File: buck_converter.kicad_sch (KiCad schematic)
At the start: 42 parts, among them IC2 LM34936RHFR, Q10 CSD15571Q2, Q11 CSD15571Q2, Q5 CSD17571Q2, Q6 CSD15571Q2, Q9 CSD17571Q2

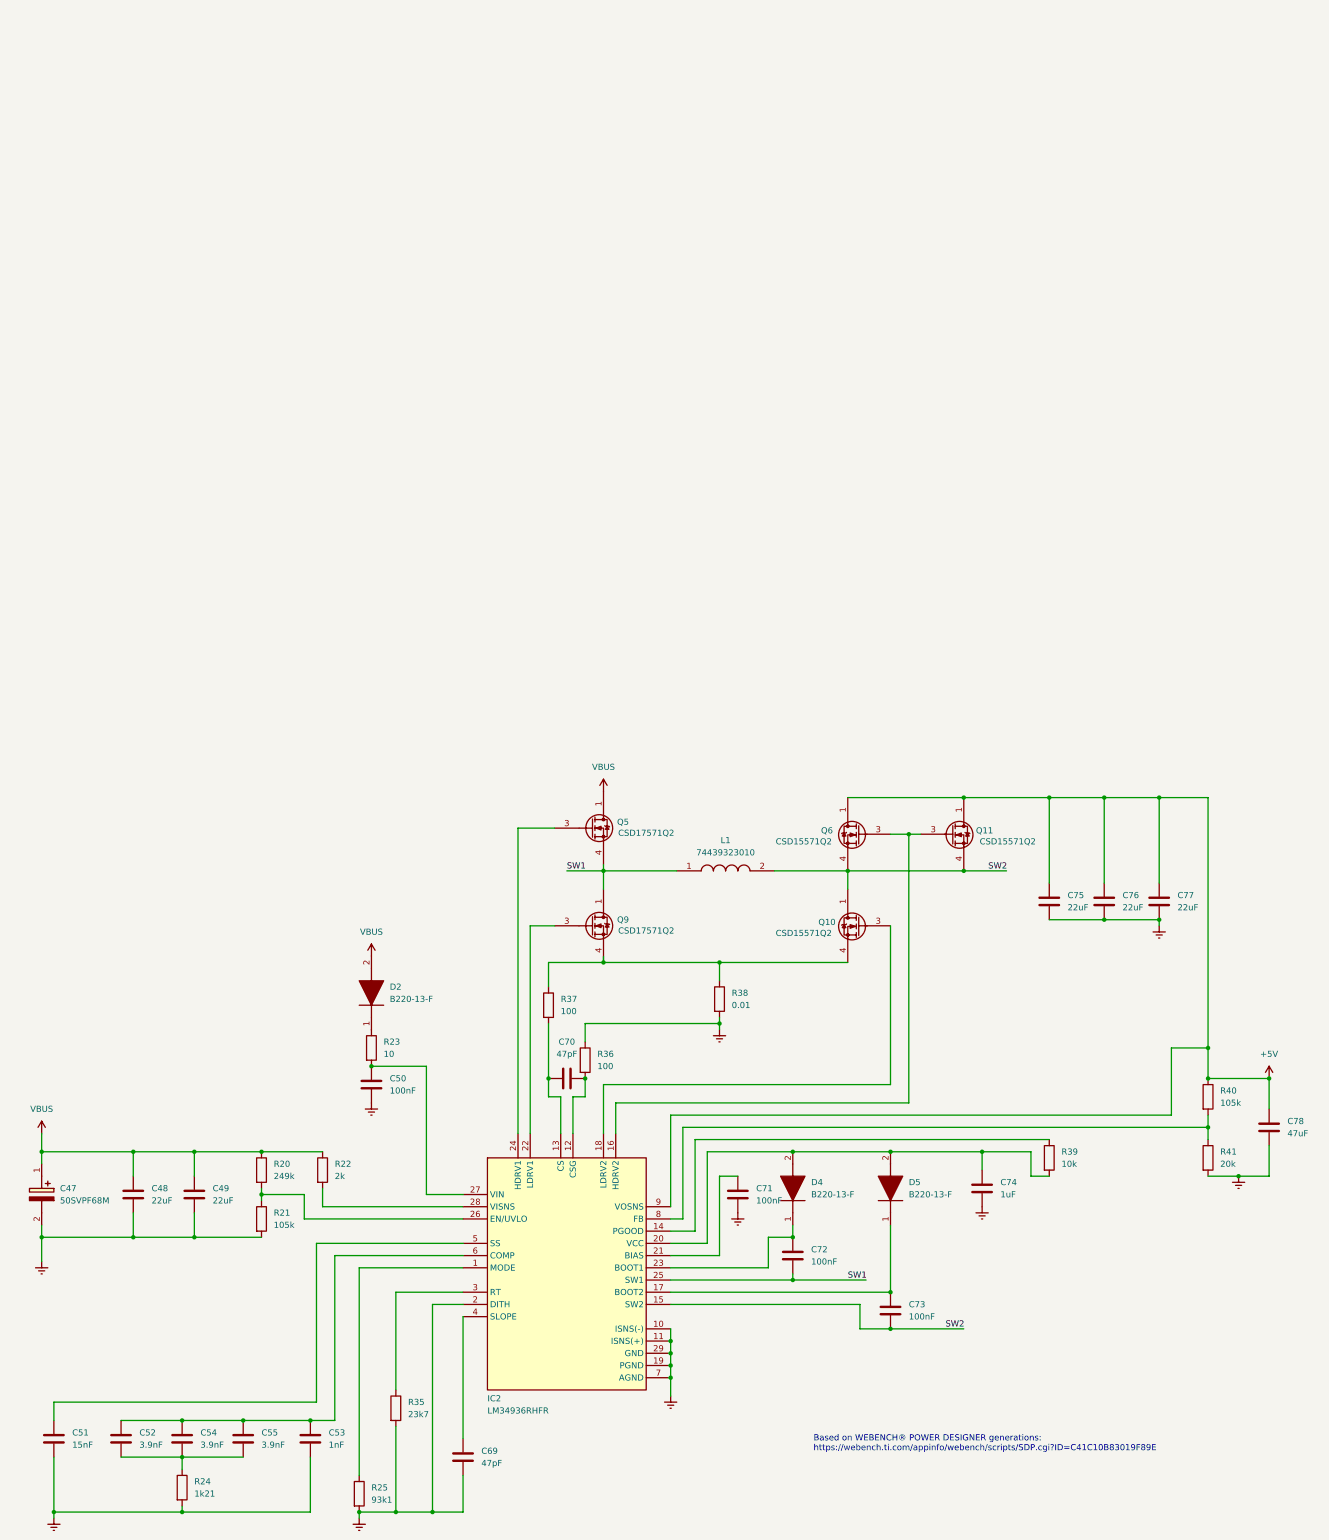
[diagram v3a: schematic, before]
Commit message: annotation and pcb outline
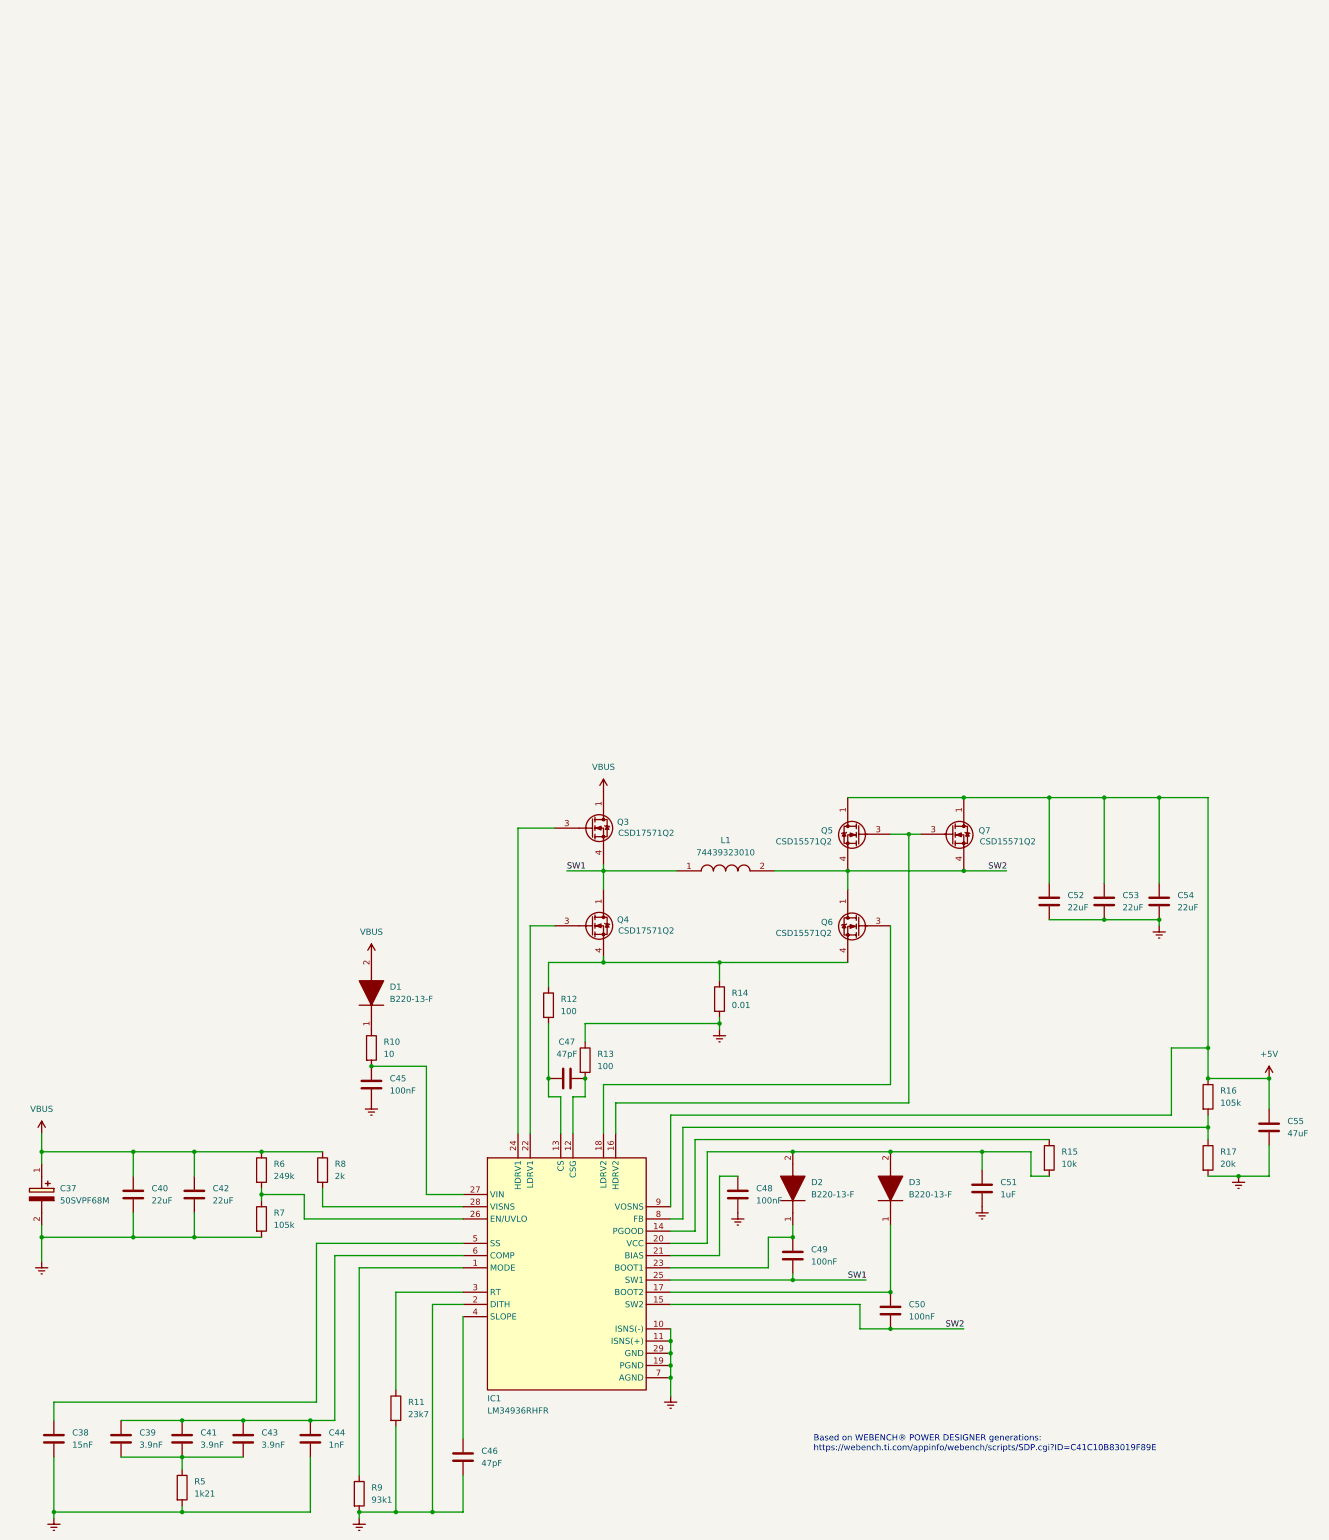
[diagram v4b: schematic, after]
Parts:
- Q5: renamed from Q6; footprint CSD15571Q2 -> CSD15571Q2:CSD15571Q2
- renumbered C47 to C37, C51 to C38, C52 to C39, C48 to C40, C54 to C41, C49 to C42, C55 to C43, C53 to C44, C50 to C45, C69 to C46, C70 to C47, C71 to C48, C72 to C49, C73 to C50, C74 to C51, C75 to C52, C76 to C53, C77 to C54, C78 to C55, D2 to D1, D4 to D2, D5 to D3, IC2 to IC1, Q5 to Q3, Q9 to Q4, Q10 to Q6, Q11 to Q7, R23 to R10, R35 to R11, R37 to R12, R36 to R13, R38 to R14, R39 to R15, R40 to R16, R41 to R17, R24 to R5, R20 to R6, R21 to R7, R22 to R8, R25 to R9

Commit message: new caps and bit of layout
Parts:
- removed C37: 50SVPF68M, 50SVPF68M:16SVF1000M, symbol 50SVPF68M:50SVPF68M
- added C37, C39: 25SVPF47M, 25SVPF47M:16SVF180M, symbol 25SVPF47M:25SVPF47M
- renumbered C39 to C40, C40 to C42, C42 to C44, C44 to C45, C45 to C46, C46 to C47, C47 to C48, C48 to C49, C49 to C50, C50 to C51, C51 to C52, C52 to C53, C53 to C54, C54 to C55, C55 to C56, R8 to R10, R9 to R8, R10 to R9
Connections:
- net GND: now also C37.2 (-), C39.2 (-)
- net VBUS: now also C37.1 (+), C39.1 (+)
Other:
- moved on the sheet: C38, C40, C41, C42, C43, C44, C45, C46, C47, C48, C49, C50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

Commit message: layout- 1st placement
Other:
- note added: "Based on WEBENCH® POWER DESIGNER generations: https://webench.ti.com/appinfo/webench/scripts/SDP.cgi?ID=7ECE0A1D317B02D5"
- note removed: "Based on WEBENCH® POWER DESIGNER generations: https://webench.ti.com/appinfo/webench/scripts/SDP.cgi?ID=C41C10B83019F89E"
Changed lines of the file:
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@@
 	(generator_version "9.0")
 	(paper "A4")
-	(text "Based on WEBENCH® POWER DESIGNER generations:\nhttps://webench.ti.com/appinfo/webench/scripts/SDP.cgi?ID=C41C10B83019F89E"
+	(text "Based on WEBENCH® POWER DESIGNER generations:\nhttps://webench.ti.com/appinfo/webench/scripts/SDP.cgi?ID=7ECE0A1D317B02D5\n"
 		(exclude_from_sim no)
 		(at 178.308 169.926 0)

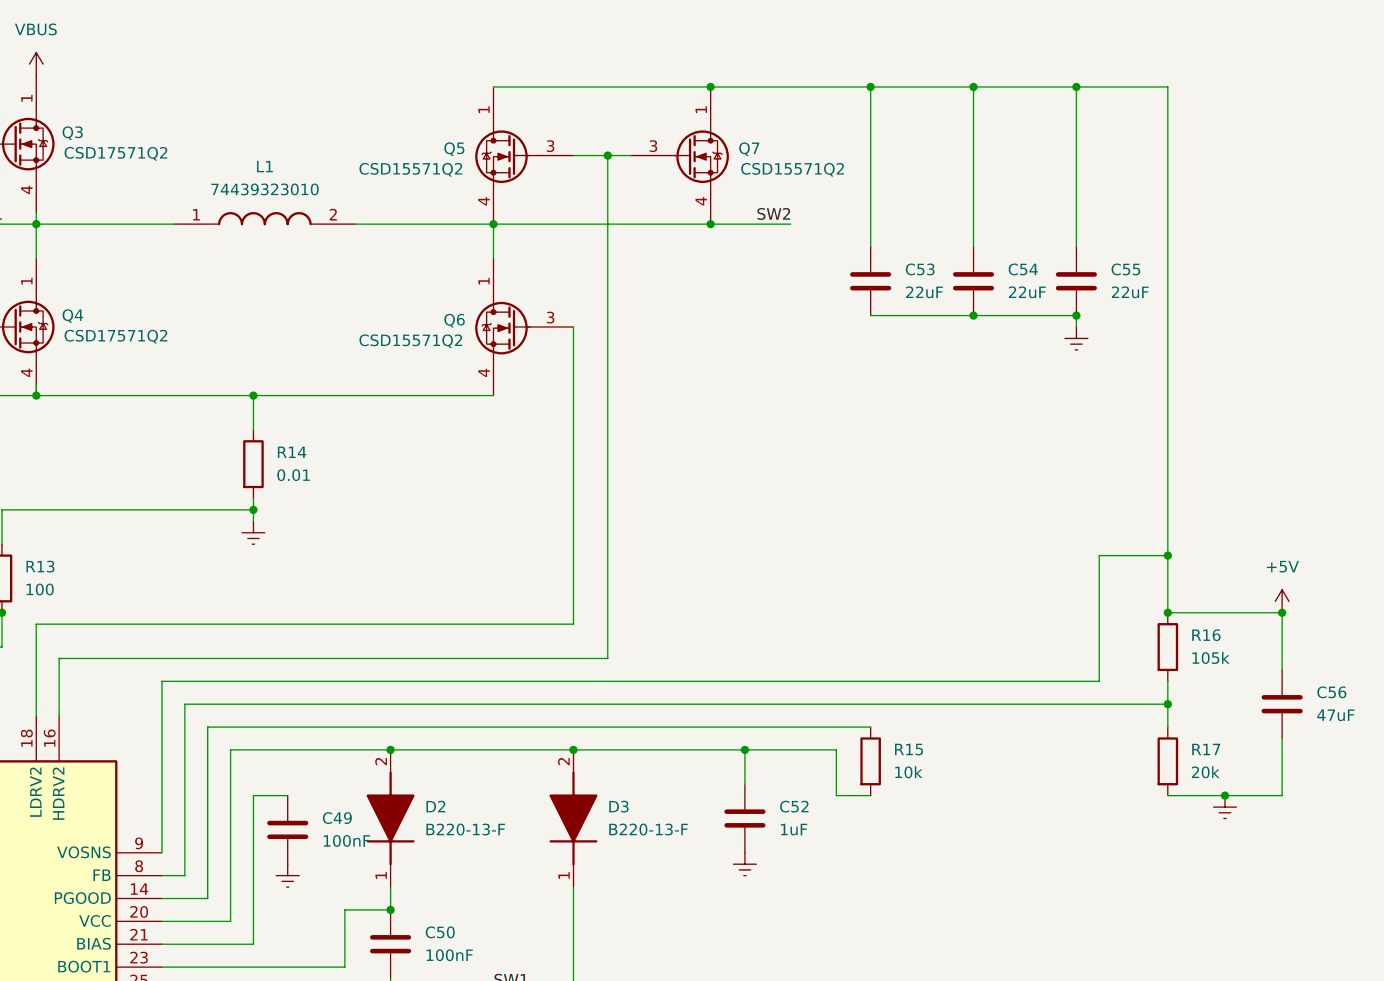
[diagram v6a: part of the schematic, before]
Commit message: added fuze
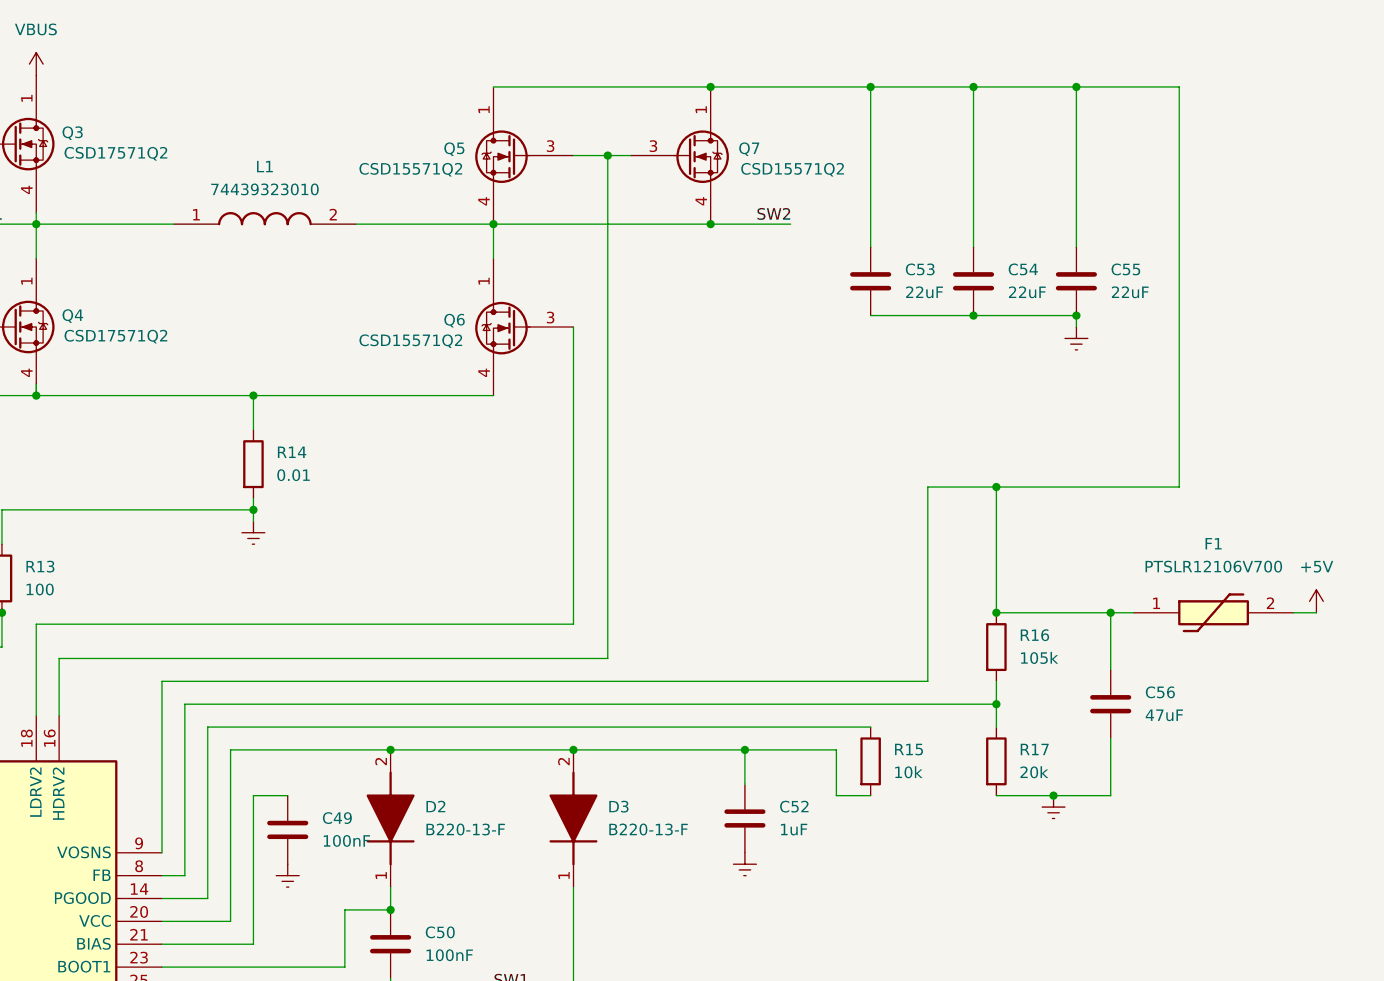
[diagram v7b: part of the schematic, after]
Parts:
- added F1: PTSLR12106V700, PTSLR12106V700, symbol PTSLR12106V700:PTSLR12106V700
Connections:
- net +5V: now also F1.2; no longer C53.1, C54.1, C55.1, C56.1, IC1.9 (VOSNS), Q5.1 (D), Q5.2 (D), Q5.5 (D), Q5.6 (D), Q5.7 (D), Q7.1 (D), Q7.2 (D), Q7.5 (D), Q7.6 (D), Q7.7 (D), R16.1
- new net: C53.1, C54.1, C55.1, C56.1, F1.1, IC1.9 (VOSNS), Q5.1 (D), Q5.2 (D), Q5.5 (D), Q5.6 (D), Q5.7 (D), Q7.1 (D), Q7.2 (D), Q7.5 (D), Q7.6 (D), Q7.7 (D), R16.1
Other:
- moved on the sheet: C56, R16, R17
